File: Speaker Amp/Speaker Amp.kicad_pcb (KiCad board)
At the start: 2 copper layers, 46.4 x 52.1 mm, 56 parts, among them J1 USB_C_Receptacle_USB2.0_16P, J2 Screw_Terminal_01x02, J3 Screw_Terminal_01x02, J4 Screw_Terminal_01x02, SW1 SW_Push, SW2 SW_Push, SW3 SW_Push, U1 LD1117S33TR_SOT223, U2 PCM2704CDBR, U3 TDA7297, U4 CH221K, Y1 12M

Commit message: Speaker Amp: rename cap values .022u/.22u to 22n/220n for fab BOM compatibility
Co-Authored-By: Claude Fable 5 <noreply@anthropic.com>
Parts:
- C11, C12: value .022u -> 22n
- C13, C14: value .22u -> 220n
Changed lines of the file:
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@@
 			)
 		)
-		(property "Value" ".22u"
+		(property "Value" "220n"
 			(at 0 1.68 90)
 			(layer "F.Fab")
@@
 			)
 		)
-		(property "Value" ".022u"
+		(property "Value" "22n"
 			(at 0 1.68 90)
 			(layer "F.Fab")
@@
 			)
 		)
-		(property "Value" ".022u"
+		(property "Value" "22n"
 			(at 0 1.68 90)
 			(layer "F.Fab")
@@
 			)
 		)
-		(property "Value" ".22u"
+		(property "Value" "220n"
 			(at 0 1.68 90)
 			(layer "F.Fab")

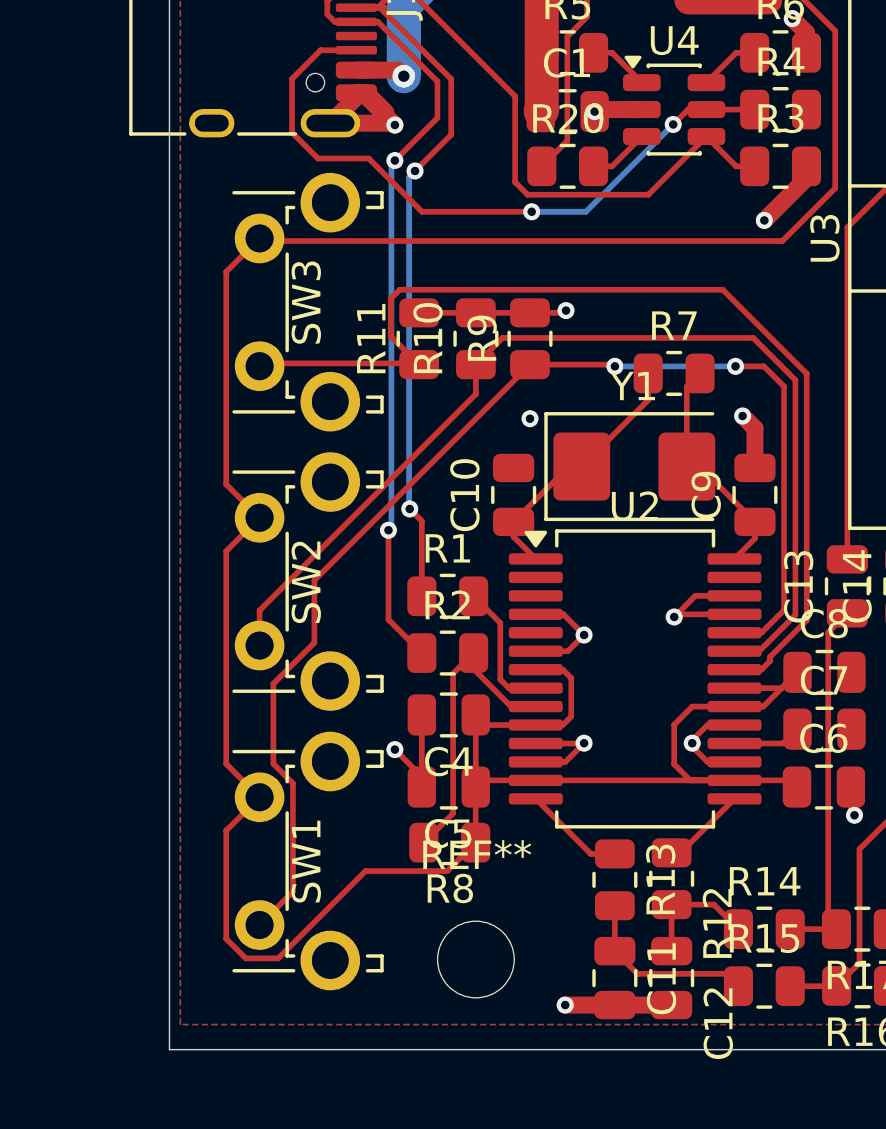
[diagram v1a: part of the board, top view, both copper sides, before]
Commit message: Speaker Amp: JLC-stockable parts - 3225 crystal, XUNPU TS-1005B SMD side buttons
Y1 swapped to 2-pin-mapped 3225 footprint (basic-part crystals); SW1-SW3
swapped to SMD side-press switches (LCSC C2856783, machine-assembled),
rotated to face the board edge with bracket anchors at the edge. 3.3V
button rail moved to a B.Cu pad-via rail; HID1/HID2 rerouted on B.Cu
around the USB differential pair. DRC: 0 errors, 0 unconnected, 0 parity.

Co-Authored-By: Claude Fable 5 <noreply@anthropic.com>
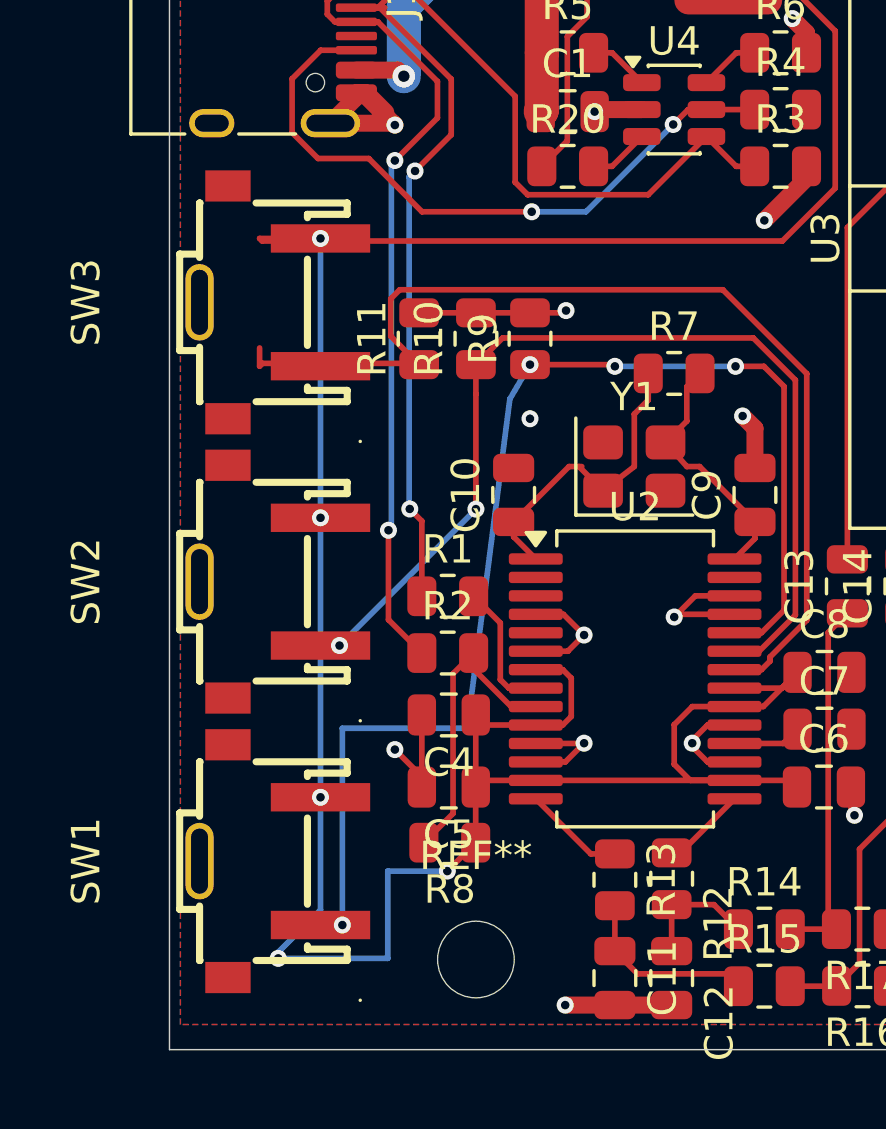
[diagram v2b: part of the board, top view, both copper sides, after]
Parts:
- SW1, SW2, SW3: footprint Button_Switch_THT:SW_Tactile_SPST_Angled_PTS645Vx58-2LFS -> SpeakerAmp:SW_TS-1005B_2PinMapped
- Y1: footprint Crystal:Crystal_SMD_5032-2Pin_5.0x3.2mm -> SpeakerAmp:Crystal_SMD_3225_2PinMapped
- moved SW1 2.25 mm to (70.5, 77.2)
- moved SW2 2.25 mm to (70.5, 67.3)
- moved SW3 2.25 mm to (70.5, 57.5)
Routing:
- net Net-(U2-XTO): track 9.09 -> 10.9 mm
- net Net-(U2-HID1/MC): track 36.3 -> 35.1 mm, vias 0 -> 2
- net /+3.3V: track 113.3 -> 114.0 mm, vias 0 -> 5
- net Net-(U2-XTI): track 8.28 -> 8.88 mm
- net Net-(U2-HID2/MD): track 43.5 -> 43.7 mm, vias 2 -> 4

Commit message: Speaker Amp: user trace cleanup, zones refilled, renders and fab package regenerated
Co-Authored-By: Claude Fable 5 <noreply@anthropic.com>
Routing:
- net /+3.3V: track 114.0 -> 109.0 mm, vias 5 -> 4
- net Net-(U2-HID2/MD): track 43.7 -> 41.7 mm
- net GND: track 48.2 -> 50.1 mm
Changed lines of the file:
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@@
+	)
+	(segment
+		(start 79.434 63.33)
+		(end 80.75 62.014)
+		(width 0.2)
+		(layer "F.Cu")
+		(net "GND")
 	)
 	(segment
@@
 	)
 	(segment
-		(start 77.0965 77.53)
-		(end 78.0965 76.53)
+		(start 74.880002 79)
+		(end 75.6265 79)
 		(width 0.2)
 		(layer "F.Cu")
@@
 		(start 85.657 74.335)
 		(end 85.09 73.768)
+		(width 0.2)
+		(layer "F.Cu")
+		(net "/+3.3V")
+	)
+	(segment
+		(start 75.6265 79)
+		(end 78.0965 76.53)
 		(width 0.2)
 		(layer "F.Cu")
@@
 	)
 	(via
-		(at 71.141 80.605)
+		(at 74.880002 79)
 		(size 0.6)
 		(drill 0.3)
@@
 	)
 	(via
-		(at 77.097 77.53)
-		(size 0.6)
-		(drill 0.3)
-		(layers "F.Cu" "B.Cu")
-		(net "/+3.3V")
-	)
-	(via
 		(at 72.63 65.085)
 		(size 0.6)
@@
 	(segment
 		(start 72.63 74.93)
-		(end 72.63 78.9)
-		(width 0.2)
-		(layer "B.Cu")
-		(net "/+3.3V")
-	)
-	(segment
-		(start 72.63 78.9)
-		(end 71.141 80.389)
-		(width 0.2)
-		(layer "B.Cu")
-		(net "/+3.3V")
-	)
-	(segment
-		(start 75 80.605)
-		(end 75 77.53)
+		(end 72.63 79.508529)
+		(width 0.2)
+		(layer "B.Cu")
+		(net "/+3.3V")
+	)
+	(segment
+		(start 73.151471 80.03)
+		(end 73.850002 80.03)
+		(width 0.2)
+		(layer "B.Cu")
+		(net "/+3.3V")
+	)
+	(segment
+		(start 73.850002 80.03)
+		(end 74.880002 79)
 		(width 0.2)
 		(layer "B.Cu")
@@
 	)
 	(segment
-		(start 71.141 80.605)
-		(end 75 80.605)
-		(width 0.2)
-		(layer "B.Cu")
-		(net "/+3.3V")
-	)
-	(segment
-		(start 71.141 80.389)
-		(end 71.141 80.605)
-		(width 0.2)
-		(layer "B.Cu")
-		(net "/+3.3V")
-	)
-	(segment
-		(start 75 77.53)
-		(end 77.097 77.53)
+		(start 72.63 79.508529)
+		(end 73.151471 80.03)
 		(width 0.2)
 		(layer "B.Cu")
@@
 	)
 	(segment
-		(start 77.8 72.5)
-		(end 73.4 72.5)
+		(start 79.41 64.34)
+		(end 79.41 60.29)
 		(width 0.2)
 		(layer "B.Cu")
@@
 	)
 	(segment
-		(start 73.4 72.5)
-		(end 73.4 79.43)
-		(width 0.2)
-		(layer "B.Cu")
-		(net "Net-(U2-HID2{slash}MD)")
-	)
-	(segment
-		(start 79.3 60.9)
-		(end 77.8 72.5)
-		(width 0.2)
-		(layer "B.Cu")
-		(net "Net-(U2-HID2{slash}MD)")
-	)
-	(segment
-		(start 80.01 59.69)
-		(end 79.3 60.9)
+		(start 73.4 70.35)
+		(end 79.41 64.34)
 		(width 0.2)
 		(layer "B.Cu")
@@
 		(width 0.2)
 		(layer "B.Cu")
+		(net "Net-(U2-HID2{slash}MD)")
+	)
+	(segment
+		(start 79.41 60.29)
+		(end 80.01 59.69)
+		(width 0.2)
+		(layer "B.Cu")
+		(net "Net-(U2-HID2{slash}MD)")
+	)
+	(segment
+		(start 73.4 79.43)
+		(end 73.4 70.35)
+		(width 0.2)
+		(layer "B.Cu")
